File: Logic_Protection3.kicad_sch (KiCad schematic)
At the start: 10 parts

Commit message: VER2.2: все изменения в списке изменений
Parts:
- D6, D7: value ADM3485E -> ~; Description P/N (none) -> RS485; Product Name (none) -> SN65HVD3082EDR

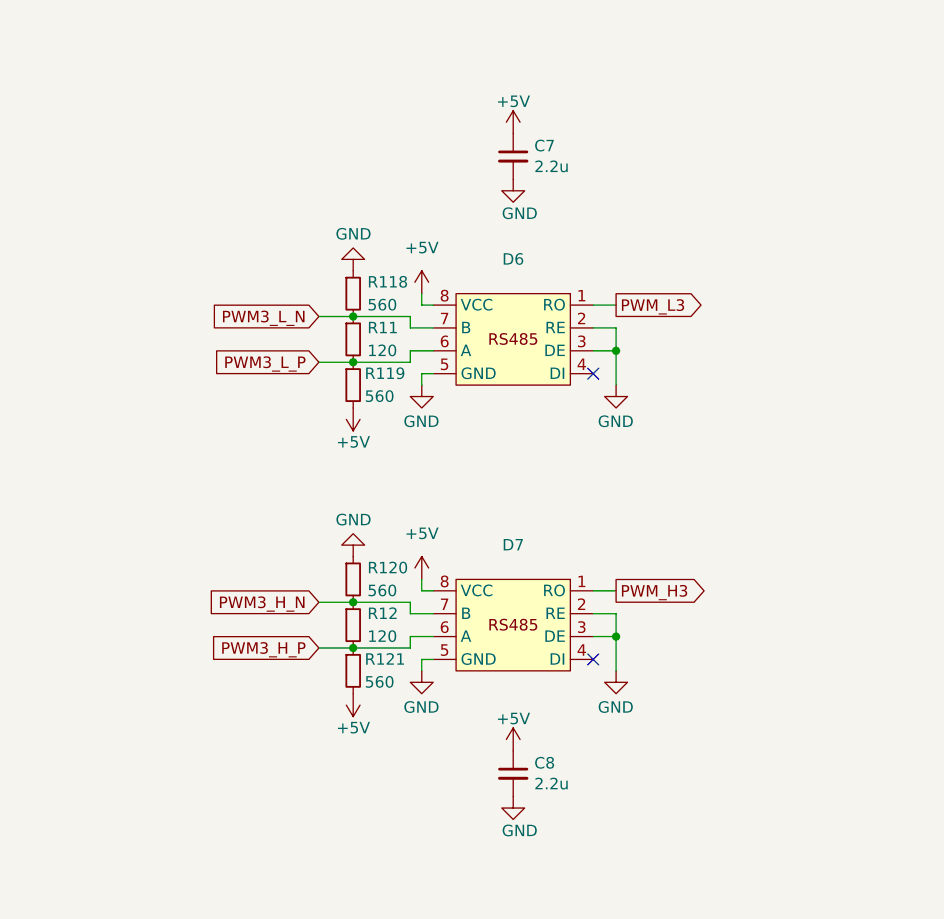
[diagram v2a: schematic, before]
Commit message: VER2.2: добавил фильтры на вход ШИМа и обновил все доки
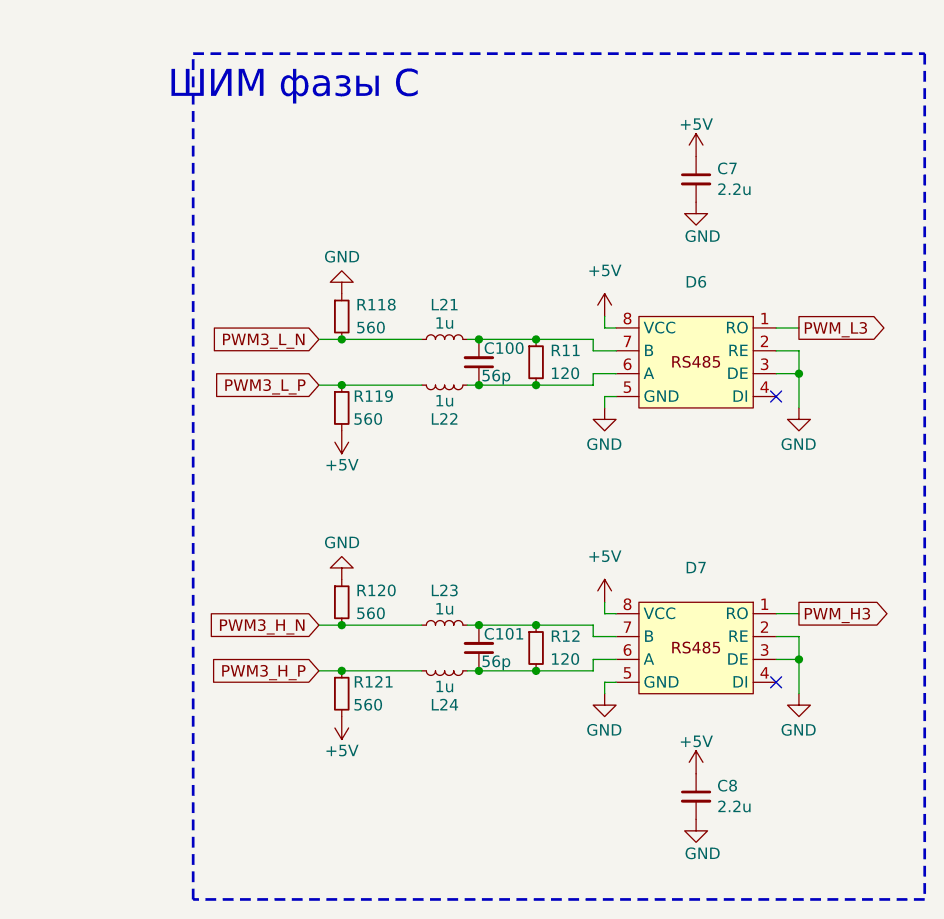
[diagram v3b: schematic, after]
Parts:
- added C100, C101: 56p, Capacitor_SMD:C_0805_2012Metric_Pad1.18x1.45mm_HandSolder, symbol Device:C_Small
- added L21, L22, L23, L24: 1u, Inductor_SMD:L_0603_1608Metric_Pad1.05x0.95mm_HandSolder, symbol Device:L_Small
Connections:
- net PWM3_H_N: now also L23.1; no longer D7.7 (B), R12.1
- net PWM3_H_P: now also L24.2; no longer D7.6 (A), R12.2
- net PWM3_L_N: now also L21.1; no longer D6.7 (B), R11.1
- net PWM3_L_P: now also L22.2; no longer D6.6 (A), R11.2
- new net: C101.1, D7.6 (A), L24.1, R12.2
- new net: C101.2, D7.7 (B), L23.2, R12.1
- new net: C100.1, D6.6 (A), L22.1, R11.2
- new net: C100.2, D6.7 (B), L21.2, R11.1
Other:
- note added: "ШИМ фазы C"
- company: (none) -> ООО "ЭТТ"
- moved on the sheet: C7, C8, D6, D7, R11, R118, R119, R12, R120, R121

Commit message: VER2.2.1: создал папку для производственных доков
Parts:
- C100, C101, C7, C8: Description P/N (none) -> Capacitor SMD 25+V
- R11, R118, R119, R12, R120, R121: Description P/N (none) -> Resistor SMD
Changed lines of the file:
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@@
 			)
 		)
-		(property "Description P/N" ""
+		(property "Description P/N" "Resistor SMD"
 			(at 132.08 93.98 0)
 			(effects
@@
 			)
 		)
-		(property "Description P/N" ""
+		(property "Description P/N" "Capacitor SMD 25+V"
 			(at 147.32 120.65 0)
 			(effects
@@
 			)
 		)
-		(property "Description P/N" ""
+		(property "Description P/N" "Resistor SMD"
 			(at 153.67 120.65 0)
 			(effects
@@
 			)
 		)
-		(property "Description P/N" ""
+		(property "Description P/N" "Resistor SMD"
 			(at 132.08 125.73 0)
 			(effects
@@
 			)
 		)
-		(property "Description P/N" ""
+		(property "Description P/N" "Resistor SMD"
 			(at 132.08 115.57 0)
 			(effects
@@
 			)
 		)
-		(property "Description P/N" ""
+		(property "Description P/N" "Capacitor SMD 25+V"
 			(at 147.32 88.9 0)
 			(effects
@@
 			)
 		)
-		(property "Description P/N" ""
+		(property "Description P/N" "Capacitor SMD 25+V"
 			(at 171.45 137.16 0)
 			(effects
@@
 			)
 		)
-		(property "Description P/N" ""
+		(property "Description P/N" "Capacitor SMD 25+V"
 			(at 171.45 68.58 0)
 			(effects
@@
 			)
 		)
-		(property "Description P/N" ""
+		(property "Description P/N" "Resistor SMD"
 			(at 132.08 83.82 0)
 			(effects
@@
 			)
 		)
-		(property "Description P/N" ""
+		(property "Description P/N" "Resistor SMD"
 			(at 153.67 88.9 0)
 			(effects

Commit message: VER2.2.1: исправил все доки
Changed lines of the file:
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@@
 		(date "2025-06-04")
 		(company "ООО \"ЭТТ\"")
+		(comment 1 "НВЦТ.EVP150-2-1.2000.120_v1 Э3")
 	)
 	(rectangle
@@
 					(size 1.27 1.27)
 				)
+				(hide yes)
 			)
 		)
@@
 					(size 1.27 1.27)
 				)
+				(hide yes)
 			)
 		)
@@
 					(size 1.27 1.27)
 				)
+				(hide yes)
 			)
 		)
@@
 					(size 1.27 1.27)
 				)
+				(hide yes)
 			)
 		)
@@
 					(size 1.27 1.27)
 				)
+				(hide yes)
 			)
 		)
@@
 					(size 1.27 1.27)
 				)
+				(hide yes)
 			)
 		)
@@
 					(size 1.27 1.27)
 				)
+				(hide yes)
 			)
 		)
@@
 					(size 1.27 1.27)
 				)
+				(hide yes)
 			)
 		)
@@
 					(size 1.27 1.27)
 				)
+				(hide yes)
 			)
 		)
@@
 					(size 1.27 1.27)
 				)
-			)
-		)
+				(hide yes)
+			)
+		)

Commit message: VER2.2: исправил ошибки в доках
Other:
- moved on the sheet: C100, C101, C7, C8, D6, D7, L21, L22, L23, L24, R11, R118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
